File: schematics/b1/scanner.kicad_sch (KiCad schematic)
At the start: 1 part, among them P1 RFID-RC522

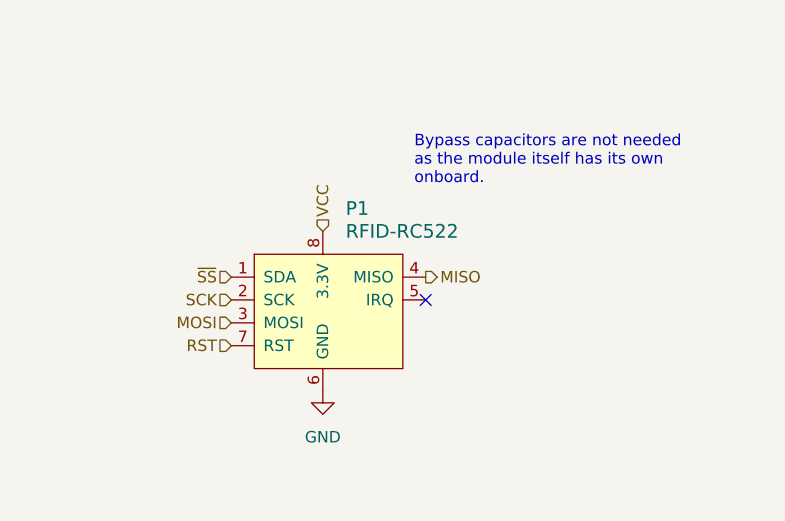
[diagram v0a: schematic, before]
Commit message: Updated Wi-Fi block with a jumper switch as a workaround.
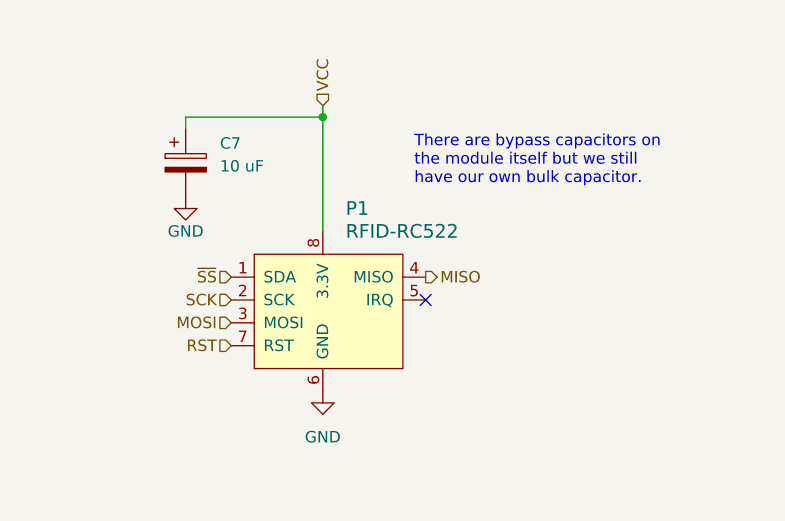
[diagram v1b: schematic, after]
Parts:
- added C7: 10 uF, symbol Device:C_Polarized
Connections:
- net GND: now also C7.2
- net VCC: now also C7.1
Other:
- note added: "There are bypass capacitors on the module itself but we still have our own bulk capacitor."
- note removed: "Bypass capacitors are not needed as the module itself has its own onboard."
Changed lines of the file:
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@@
     (comment 4 "The scanner is an RFID-RC522 module attached to the motherboard via a ribbon cable.")
   )
+  (junction (at 99.06 38.1) (diameter 0) (color 0 0 0 0)
+  )
   (no_connect (at 110.49 58.42))
-  (text "Bypass capacitors are not needed\nas the module itself has its own\nonboard."
+  (wire (pts (xy 99.06 36.83) (xy 99.06 38.1))
+    (stroke (width 0) (type default))
+  )
+  (wire (pts (xy 99.06 38.1) (xy 99.06 50.8))
+    (stroke (width 0) (type default))
+  )
+  (wire (pts (xy 83.82 38.1) (xy 83.82 39.37))
+    (stroke (width 0) (type default))
+  )
+  (wire (pts (xy 83.82 38.1) (xy 99.06 38.1))
+    (stroke (width 0) (type default))
+  )
+  (text "There are bypass capacitors on\nthe module itself but we still\nhave our own bulk capacitor."
     (at 109.22 45.72 0)
     (effects (font (size 1.27 1.27)) (justify left bottom))
   )
-  (hierarchical_label "VCC" (shape input) (at 99.06 50.8 90) (fields_autoplaced)
+  (hierarchical_label "VCC" (shape input) (at 99.06 36.83 90) (fields_autoplaced)
     (effects (font (size 1.27 1.27)) (justify left))
   )
@@
         )
       )
+    )
+  )
+  (symbol (lib_id "Device:C_Polarized") (at 83.82 43.18 0) (unit 1)
+    (in_bom yes) (on_board yes) (dnp no)
+    (property "Reference" "C7" (at 87.63 41.021 0)
+      (effects (font (size 1.27 1.27)) (justify left))
+    )
+    (property "Value" "10 uF" (at 87.63 43.561 0)
+      (effects (font (size 1.27 1.27)) (justify left))
+    )
+    (property "Footprint" "" (at 84.7852 46.99 0)
+      (effects (font (size 1.27 1.27)) hide)
+    )
+    (property "Datasheet" "~" (at 83.82 43.18 0)
+      (effects (font (size 1.27 1.27)) hide)
+    )
+    (pin "2")
+    (pin "1")
+    (instances
+      (project "b1"
+        (path "/d6142fa5-2354-4512-9919-37616259c364/64a24a3a-7315-4dfd-86dd-98547cdfac2f"
+          (reference "C7") (unit 1)
+        )
+      )
+    )
+  )
+  (symbol (lib_id "power:GND") (at 83.82 46.99 0) (unit 1)
+    (in_bom yes) (on_board yes) (dnp no)
+    (property "Reference" "#PWR012" (at 83.82 53.34 0)
+      (effects (font (size 1.27 1.27)) hide)
+    )
+    (property "Value" "GND" (at 83.82 50.8 0)
+      (effects (font (size 1.27 1.27)))
+    )
+    (property "Footprint" "" (at 83.82 46.99 0)
+      (effects (font (size 1.27 1.27)) hide)
+    )
+    (property "Datasheet" "" (at 83.82 46.99 0)
+      (effects (font (size 1.27 1.27)) hide)
+    )
+    (pin "1")
+    (instances
+      (project "b1"
+        (path "/d6142fa5-2354-4512-9919-37616259c364/64a24a3a-7315-4dfd-86dd-98547cdfac2f"
+          (reference "#PWR012") (unit 1)
+        )
+      )

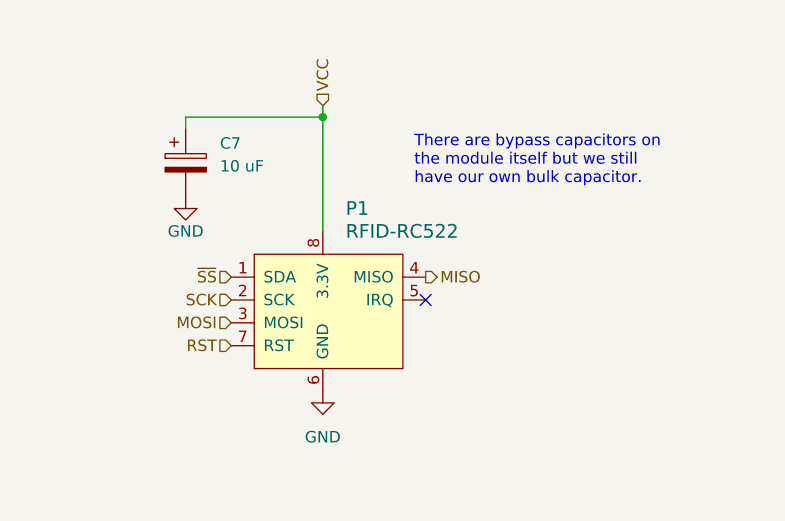
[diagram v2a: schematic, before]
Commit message: Increased bulk cap value for scanner.
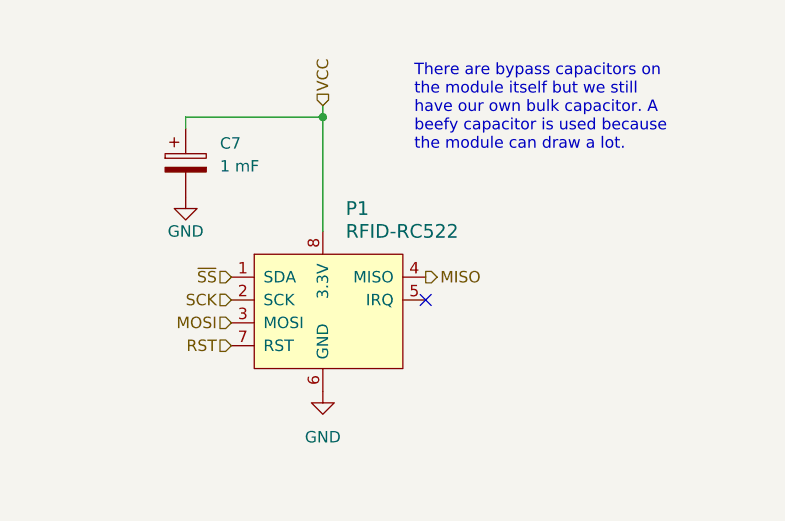
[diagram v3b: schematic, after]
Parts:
- C7: value 10 uF -> 1 mF
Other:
- note added: "There are bypass capacitors on the module itself but we still have our own bulk capacitor. A beefy capacitor is used because the module can draw a lot."
- note removed: "There are bypass capacitors on the module itself but we still have our own bulk capacitor."
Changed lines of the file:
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@@
     (stroke (width 0) (type default))
   )
-  (text "There are bypass capacitors on\nthe module itself but we still\nhave our own bulk capacitor."
-    (at 109.22 45.72 0)
+  (text "There are bypass capacitors on\nthe module itself but we still\nhave our own bulk capacitor. A\nbeefy capacitor is used because\nthe module can draw a lot."
+    (at 109.22 41.91 0)
     (effects (font (size 1.27 1.27)) (justify left bottom))
   )
@@
       (effects (font (size 1.27 1.27)) (justify left))
     )
-    (property "Value" "10 uF" (at 87.63 43.561 0)
+    (property "Value" "1 mF" (at 87.63 43.561 0)
       (effects (font (size 1.27 1.27)) (justify left))
     )

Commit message: Updated RFID scanner wiring.
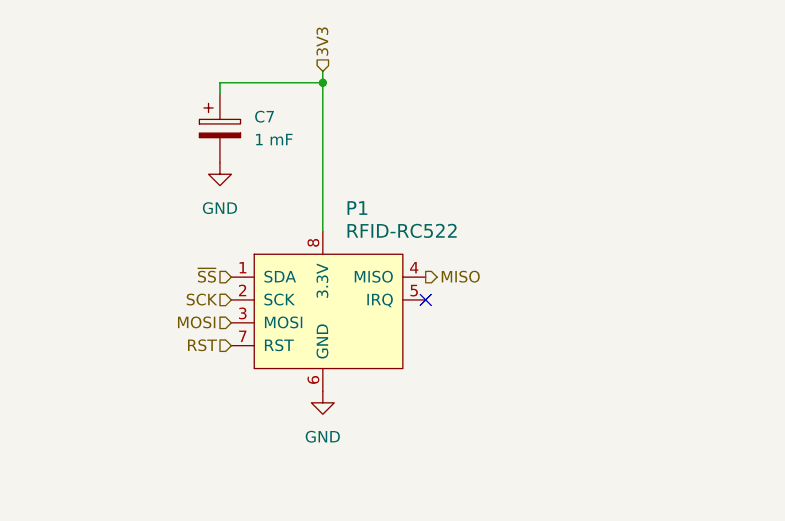
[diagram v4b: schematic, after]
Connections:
- net VCC renamed 3V3
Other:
- note removed: "There are bypass capacitors on the module itself but we still have our own bulk capacitor. A beefy capacitor is used because the module can draw a lot."
- moved on the sheet: C7
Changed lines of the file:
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@@
     (comment 4 "The scanner is an RFID-RC522 module attached to the motherboard via a ribbon cable.")
   )
-  (junction (at 99.06 38.1) (diameter 0) (color 0 0 0 0)
+  (junction (at 99.06 34.29) (diameter 0) (color 0 0 0 0)
   )
   (no_connect (at 110.49 58.42))
-  (wire (pts (xy 99.06 36.83) (xy 99.06 38.1))
+  (wire (pts (xy 99.06 33.02) (xy 99.06 34.29))
     (stroke (width 0) (type default))
   )
-  (wire (pts (xy 99.06 38.1) (xy 99.06 50.8))
+  (wire (pts (xy 99.06 34.29) (xy 99.06 50.8))
     (stroke (width 0) (type default))
   )
-  (wire (pts (xy 83.82 38.1) (xy 83.82 39.37))
+  (wire (pts (xy 87.63 34.29) (xy 87.63 35.56))
     (stroke (width 0) (type default))
   )
-  (wire (pts (xy 83.82 38.1) (xy 99.06 38.1))
+  (wire (pts (xy 87.63 34.29) (xy 99.06 34.29))
     (stroke (width 0) (type default))
   )
-  (text "There are bypass capacitors on\nthe module itself but we still\nhave our own bulk capacitor. A\nbeefy capacitor is used because\nthe module can draw a lot."
-    (at 109.22 41.91 0)
-    (effects (font (size 1.27 1.27)) (justify left bottom))
-  )
-  (hierarchical_label "VCC" (shape input) (at 99.06 36.83 90) (fields_autoplaced)
+  (hierarchical_label "3V3" (shape input) (at 99.06 33.02 90) (fields_autoplaced)
     (effects (font (size 1.27 1.27)) (justify left))
   )
@@
     )
   )
-  (symbol (lib_id "Device:C_Polarized") (at 83.82 43.18 0) (unit 1)
+  (symbol (lib_id "Device:C_Polarized") (at 87.63 39.37 0) (unit 1)
     (in_bom yes) (on_board yes) (dnp no)
-    (property "Reference" "C7" (at 87.63 41.021 0)
+    (property "Reference" "C7" (at 91.44 38.1 0)
       (effects (font (size 1.27 1.27)) (justify left))
     )
-    (property "Value" "1 mF" (at 87.63 43.561 0)
+    (property "Value" "1 mF" (at 91.44 40.64 0)
       (effects (font (size 1.27 1.27)) (justify left))
     )
-    (property "Footprint" "" (at 84.7852 46.99 0)
+    (property "Footprint" "" (at 88.5952 43.18 0)
       (effects (font (size 1.27 1.27)) hide)
     )
-    (property "Datasheet" "~" (at 83.82 43.18 0)
+    (property "Datasheet" "~" (at 87.63 39.37 0)
       (effects (font (size 1.27 1.27)) hide)
     )
@@
     )
   )
-  (symbol (lib_id "power:GND") (at 83.82 46.99 0) (unit 1)
+  (symbol (lib_id "power:GND") (at 87.63 43.18 0) (unit 1)
     (in_bom yes) (on_board yes) (dnp no)
-    (property "Reference" "#PWR017" (at 83.82 53.34 0)
+    (property "Reference" "#PWR017" (at 87.63 49.53 0)
       (effects (font (size 1.27 1.27)) hide)
     )
-    (property "Value" "GND" (at 83.82 50.8 0)
+    (property "Value" "GND" (at 87.63 48.26 0)
       (effects (font (size 1.27 1.27)))
     )
-    (property "Footprint" "" (at 83.82 46.99 0)
+    (property "Footprint" "" (at 87.63 43.18 0)
       (effects (font (size 1.27 1.27)) hide)
     )
-    (property "Datasheet" "" (at 83.82 46.99 0)
+    (property "Datasheet" "" (at 87.63 43.18 0)
       (effects (font (size 1.27 1.27)) hide)
     )

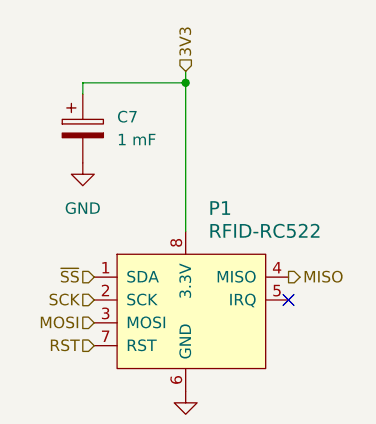
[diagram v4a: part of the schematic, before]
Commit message: Wired LoRa and added a bulk to the status block.
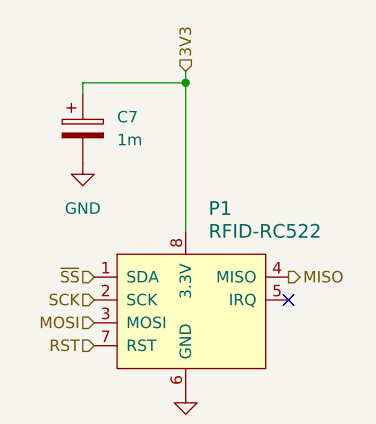
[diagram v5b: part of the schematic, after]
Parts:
- C7: value 1 mF -> 1m
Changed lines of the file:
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@@
       (effects (font (size 1.27 1.27)) (justify left))
     )
-    (property "Value" "1 mF" (at 91.44 40.64 0)
+    (property "Value" "1m" (at 91.44 40.64 0)
       (effects (font (size 1.27 1.27)) (justify left))
     )

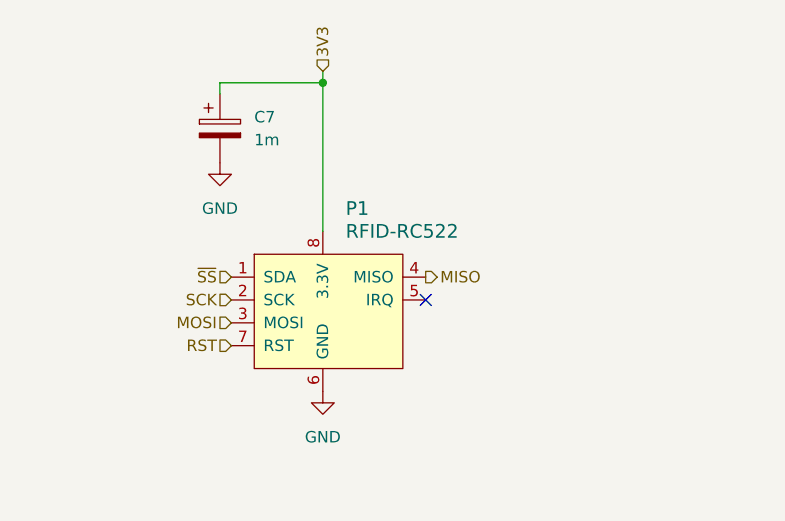
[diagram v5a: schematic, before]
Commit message: Added a bunch of test points.
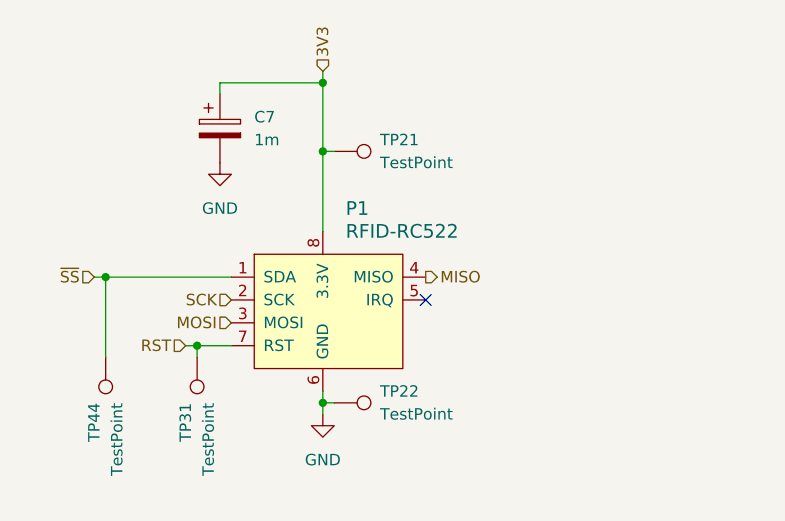
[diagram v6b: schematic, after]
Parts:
- added TP21, TP22, TP31, TP44: TestPoint, symbol Connector:TestPoint
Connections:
- net 3V3: now also TP21.1
- net GND: now also TP22.1
- net RST: now also TP31.1
- net ~{SS}: now also TP44.1
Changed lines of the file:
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@@
     (comment 4 "The scanner is an RFID-RC522 module attached to the motherboard via a ribbon cable.")
   )
+  (junction (at 99.06 41.91) (diameter 0) (color 0 0 0 0)
+  )
+  (junction (at 74.93 55.88) (diameter 0) (color 0 0 0 0)
+  )
+  (junction (at 99.06 69.85) (diameter 0) (color 0 0 0 0)
+  )
+  (junction (at 85.09 63.5) (diameter 0) (color 0 0 0 0)
+  )
   (junction (at 99.06 34.29) (diameter 0) (color 0 0 0 0)
   )
   (no_connect (at 110.49 58.42))
+  (wire (pts (xy 99.06 69.85) (xy 99.06 68.58))
+    (stroke (width 0) (type default))
+  )
   (wire (pts (xy 99.06 33.02) (xy 99.06 34.29))
     (stroke (width 0) (type default))
   )
-  (wire (pts (xy 99.06 34.29) (xy 99.06 50.8))
+  (wire (pts (xy 99.06 41.91) (xy 100.33 41.91))
+    (stroke (width 0) (type default))
+  )
+  (wire (pts (xy 74.93 55.88) (xy 88.9 55.88))
+    (stroke (width 0) (type default))
+  )
+  (wire (pts (xy 99.06 34.29) (xy 99.06 41.91))
+    (stroke (width 0) (type default))
+  )
+  (wire (pts (xy 85.09 63.5) (xy 85.09 64.77))
+    (stroke (width 0) (type default))
+  )
+  (wire (pts (xy 99.06 69.85) (xy 100.33 69.85))
+    (stroke (width 0) (type default))
+  )
+  (wire (pts (xy 83.82 63.5) (xy 85.09 63.5))
+    (stroke (width 0) (type default))
+  )
+  (wire (pts (xy 73.66 55.88) (xy 74.93 55.88))
     (stroke (width 0) (type default))
   )
   (wire (pts (xy 87.63 34.29) (xy 87.63 35.56))
+    (stroke (width 0) (type default))
+  )
+  (wire (pts (xy 99.06 41.91) (xy 99.06 50.8))
+    (stroke (width 0) (type default))
+  )
+  (wire (pts (xy 74.93 55.88) (xy 74.93 64.77))
+    (stroke (width 0) (type default))
+  )
+  (wire (pts (xy 85.09 63.5) (xy 88.9 63.5))
+    (stroke (width 0) (type default))
+  )
+  (wire (pts (xy 99.06 71.12) (xy 99.06 69.85))
     (stroke (width 0) (type default))
   )
@@
     (effects (font (size 1.27 1.27)) (justify right))
   )
-  (hierarchical_label "~{SS}" (shape input) (at 88.9 55.88 180) (fields_autoplaced)
+  (hierarchical_label "~{SS}" (shape input) (at 73.66 55.88 180) (fields_autoplaced)
     (effects (font (size 1.27 1.27)) (justify right))
   )
@@
     (effects (font (size 1.27 1.27)) (justify right))
   )
-  (hierarchical_label "RST" (shape input) (at 88.9 63.5 180) (fields_autoplaced)
+  (hierarchical_label "RST" (shape input) (at 83.82 63.5 180) (fields_autoplaced)
     (effects (font (size 1.27 1.27)) (justify right))
   )
   (hierarchical_label "MISO" (shape output) (at 110.49 55.88 0) (fields_autoplaced)
     (effects (font (size 1.27 1.27)) (justify left))
+  )
+  (symbol (lib_id "Connector:TestPoint") (at 74.93 64.77 180) (unit 1)
+    (in_bom yes) (on_board yes) (dnp no)
+    (property "Reference" "TP44" (at 73.66 69.85 90)
+      (effects (font (size 1.27 1.27)) (justify left))
+    )
+    (property "Value" "TestPoint" (at 76.2 69.85 90)
+      (effects (font (size 1.27 1.27)) (justify left))
+    )
+    (property "Footprint" "" (at 69.85 64.77 0)
+      (effects (font (size 1.27 1.27)) hide)
+    )
+    (property "Datasheet" "~" (at 69.85 64.77 0)
+      (effects (font (size 1.27 1.27)) hide)
+    )
+    (pin "1")
+    (instances
+      (project "b1"
+        (path "/d6142fa5-2354-4512-9919-37616259c364/64a24a3a-7315-4dfd-86dd-98547cdfac2f"
+          (reference "TP44") (unit 1)
+        )
+      )
+    )
   )
   (symbol (lib_id "RC522:RFID-RC522-MODULE") (at 107.95 80.01 0) (unit 1)
@@
     )
   )
-  (symbol (lib_id "power:GND") (at 99.06 68.58 0) (unit 1)
-    (in_bom yes) (on_board yes) (dnp no) (fields_autoplaced)
-    (property "Reference" "#PWR018" (at 99.06 74.93 0)
-      (effects (font (size 1.27 1.27)) hide)
-    )
-    (property "Value" "GND" (at 99.06 73.66 0)
+  (symbol (lib_id "power:GND") (at 99.06 71.12 0) (unit 1)
+    (in_bom yes) (on_board yes) (dnp no) (fields_autoplaced)
+    (property "Reference" "#PWR018" (at 99.06 77.47 0)
+      (effects (font (size 1.27 1.27)) hide)
+    )
+    (property "Value" "GND" (at 99.06 76.2 0)
       (effects (font (size 1.27 1.27)))
     )
-    (property "Footprint" "" (at 99.06 68.58 0)
-      (effects (font (size 1.27 1.27)) hide)
-    )
-    (property "Datasheet" "" (at 99.06 68.58 0)
+    (property "Footprint" "" (at 99.06 71.12 0)
+      (effects (font (size 1.27 1.27)) hide)
+    )
+    (property "Datasheet" "" (at 99.06 71.12 0)
       (effects (font (size 1.27 1.27)) hide)
     )
@@
         )
       )
+    )
+  )
+  (symbol (lib_id "Connector:TestPoint") (at 85.09 64.77 180) (unit 1)
+    (in_bom yes) (on_board yes) (dnp no)
+    (property "Reference" "TP31" (at 83.82 69.85 90)
+      (effects (font (size 1.27 1.27)) (justify left))
+    )
+    (property "Value" "TestPoint" (at 86.36 69.85 90)
+      (effects (font (size 1.27 1.27)) (justify left))
+    )
+    (property "Footprint" "" (at 80.01 64.77 0)
+      (effects (font (size 1.27 1.27)) hide)
+    )
+    (property "Datasheet" "~" (at 80.01 64.77 0)
+      (effects (font (size 1.27 1.27)) hide)
+    )
+    (pin "1")
+    (instances
+      (project "b1"
+        (path "/d6142fa5-2354-4512-9919-37616259c364/64a24a3a-7315-4dfd-86dd-98547cdfac2f"
+          (reference "TP31") (unit 1)
+        )
+      )
+    )
+  )
+  (symbol (lib_id "Connector:TestPoint") (at 100.33 41.91 270) (unit 1)
+    (in_bom yes) (on_board yes) (dnp no) (fields_autoplaced)
+    (property "Reference" "TP21" (at 105.41 40.64 90)
+      (effects (font (size 1.27 1.27)) (justify left))
+    )
+    (property "Value" "TestPoint" (at 105.41 43.18 90)
+      (effects (font (size 1.27 1.27)) (justify left))
+    )
+    (property "Footprint" "" (at 100.33 46.99 0)
+      (effects (font (size 1.27 1.27)) hide)
+    )
+    (property "Datasheet" "~" (at 100.33 46.99 0)
+      (effects (font (size 1.27 1.27)) hide)
+    )
+    (pin "1")
+    (instances
+      (project "b1"
+        (path "/d6142fa5-2354-4512-9919-37616259c364/64a24a3a-7315-4dfd-86dd-98547cdfac2f"
+          (reference "TP21") (unit 1)
+        )
+      )
+    )
+  )
+  (symbol (lib_id "Connector:TestPoint") (at 100.33 69.85 270) (unit 1)
+    (in_bom yes) (on_board yes) (dnp no) (fields_autoplaced)
+    (property "Reference" "TP22" (at 105.41 68.58 90)
+      (effects (font (size 1.27 1.27)) (justify left))
+    )
+    (property "Value" "TestPoint" (at 105.41 71.12 90)
+      (effects (font (size 1.27 1.27)) (justify left))
+    )
+    (property "Footprint" "" (at 100.33 74.93 0)
+      (effects (font (size 1.27 1.27)) hide)
+    )
+    (property "Datasheet" "~" (at 100.33 74.93 0)
+      (effects (font (size 1.27 1.27)) hide)
+    )
+    (pin "1")
+    (instances
+      (project "b1"
+        (path "/d6142fa5-2354-4512-9919-37616259c364/64a24a3a-7315-4dfd-86dd-98547cdfac2f"
+          (reference "TP22") (unit 1)
+        )
+      )
